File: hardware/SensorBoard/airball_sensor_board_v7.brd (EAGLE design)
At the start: 139.7 x 38.1 mm, 27 parts, among them J1 FEMALE 2x3

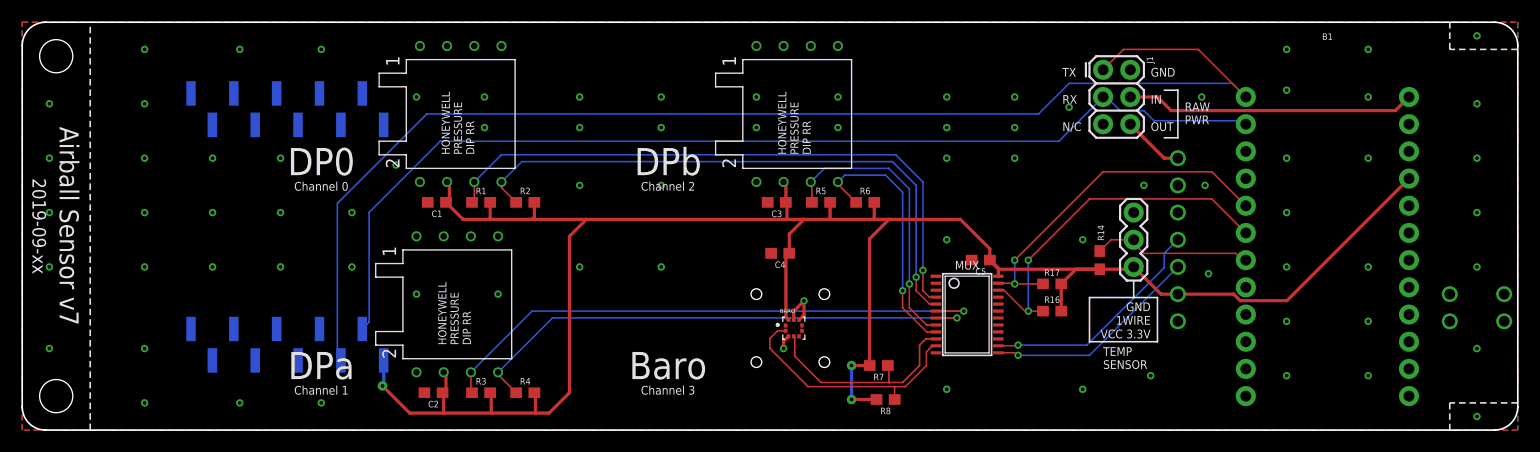
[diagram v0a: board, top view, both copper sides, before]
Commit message: Changed use of Bosch BMP388 sensor so that we are using the Adafruit breakout board instead of soldering the sensor on directly. This saves us some finicky SMT work.
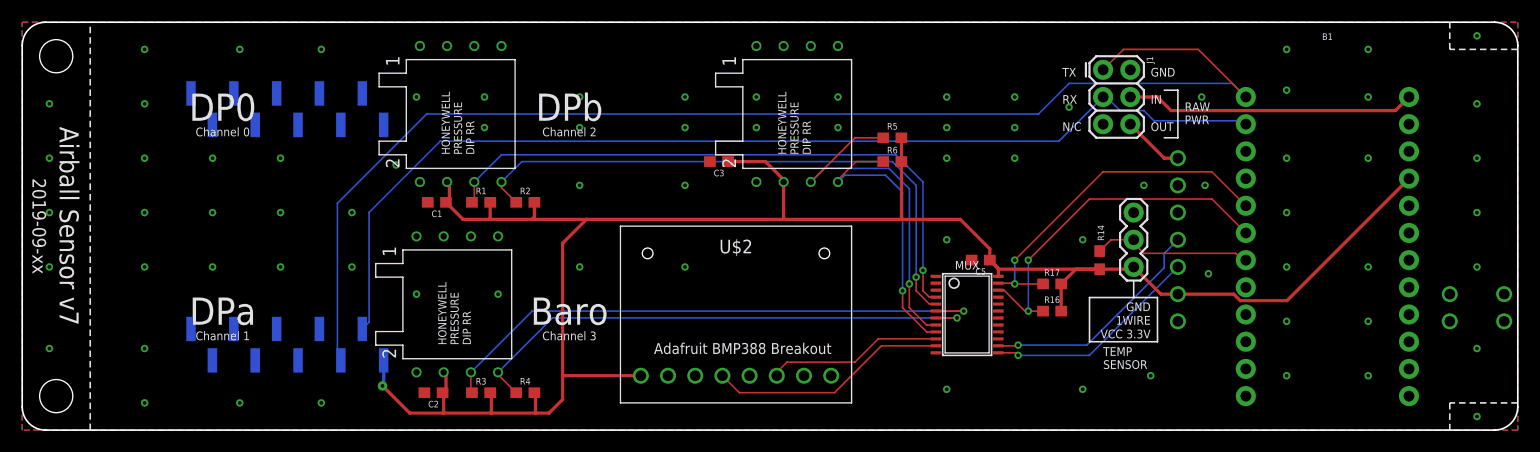
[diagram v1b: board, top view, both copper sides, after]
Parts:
- removed BARO: BMP388, BMP388:PQFN50P200X200X80-10N
- removed C4: 0.1uF, SparkFun-Capacitors:0603
- removed R7, R8: 4.7k, SparkFun-Resistors:0603
- added U$2: ADAFRUIT_BMP388_BREAKOUT, airball:ADAFRUIT_BMP388_BREAKOUT
- moved R5 8.99 mm to (81.3, 27.3)
- moved C3 6.61 mm to (65.1, 25.1)
- moved R6 4.58 mm to (81.3, 25.1)
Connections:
- removed net VDDIO: BARO.1
- net GND: now also U$2.P$3; no longer BARO.3, BARO.8, BARO.9, C4.2
- net SCL_BMP_BARO: now also U$2.P$4; no longer BARO.2, R8.1
- net SDA_BMP_BARO: now also U$2.P$6; no longer BARO.4, R7.1
- net VCC_3V3: now also U$2.P$1; no longer BARO.10, C4.1, R7.2, R8.2
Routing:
- net VCC_3V3: track 198.7 -> 184.3 mm, vias 3 -> 1
- net SDA_DPB: track 26.7 -> 33.3 mm
- net GND: track 5.48 -> 0.00 mm, vias 8 -> 6
- net SDA_BMP_BARO: track 20.5 -> 16.5 mm
- net SCL_DPB: track 24.4 -> 26.9 mm
- net SCL_BMP_BARO: track 23.7 -> 22.4 mm
